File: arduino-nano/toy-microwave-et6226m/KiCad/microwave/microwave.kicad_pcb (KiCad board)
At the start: 4 copper layers, 76.2 x 165.1 mm, 60 parts, among them J1 Screw_Terminal_01x04, J2 Screw_Terminal_01x04, U1 AP63205WU, U2 CA56-12EWA

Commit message: fix(toy-microwave-et6226m): swap to a common-cathode display and drive the buzzer through a MOSFET
- What: U2 becomes CC56-12SURKWA, BZ1 moves low-side behind AO3400A Q2 with R9/R10 and SS14 flyback D18, D1-D16 are valued 1N4148W, U5 loads from the shared embedded library, and the BOM export is regenerated.
- Why: the ET6226M sources segments and sinks grids so a common-anode display never lights, and the 42 ohm coil drew about 119 mA from a pin rated 40 mA.
- How: pin-for-pin display swap on the same footprint, a gate-resistor and pull-down MOSFET stage clamped to +5V, and a project sym-lib-table pointing at kicad/embedded.kicad_sym.
- Benefit: the display lights, the buzzer no longer overloads D10, and ERC and DRC run clean.
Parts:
- added D18: SS14, Diode_SMD:D_SMA, B.Cu at (46.7, 29.2)
- added Q2: AO3400A, Package_TO_SOT_SMD:SOT-23, B.Cu at (41.7, 28.9)
- added R10: 4.7k, Resistor_SMD:R_0805_2012Metric_Pad1.20x1.40mm_HandSolder, B.Cu at (37.6, 30.3)
- added R9: 100, Resistor_SMD:R_0805_2012Metric_Pad1.20x1.40mm_HandSolder, B.Cu at (37.6, 27.9)
- D1, D10, D11, D12, D13, D14, D15, D16, D2, D3, D4, D5, D6, D7, D8, D9: value D_Small -> 1N4148W
- U2: value CA56-12EWA -> CC56-12SURKWA; footprint Display_7Segment:CA56-12EWA -> Display_7Segment:CA56-12SURKWA
- U5: value ~ -> ET6226M
- moved BZ1 7.33 mm to (59.7, 28.7), turned to 180 degrees
- moved U2 0.10 mm to (50.8, 55.6)
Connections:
- BZ1 pad 1: CTRL_BUZZER -> +5V
- BZ1 pad 2: GND -> Net-(BZ1--)
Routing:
- net +5V: track 137.0 -> 171.0 mm
- net CTRL_BUZZER: track 169.4 -> 153.6 mm, vias 0 -> 1
- net Net-(BZ1--): track 0.00 -> 12.0 mm
- net Net-(Q2-G): track 0.00 -> 4.51 mm

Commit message: refactor(toy-microwave-et6226m): resize the board to 3.0 x 6.5 in and place the display and keys to the enclosure template
- What: resizes the board outline to 3000 x 6500 mil and moves U2 (display) and MX1-MX16 (keys) to the positions in the imported enclosure DXF, with the schematic and project files resaved.
- Why: the enclosure template fixes where the display window and key cutouts sit, so the board has to match it.
- How: imported the template DXF as a reference and placed each part to its drawn position, keys on the 750 mil MX pitch.
- Benefit: display and key placement match the enclosure 1:1.
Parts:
- moved H1 13.0 mm to (98.1, 187.0)
- moved H2 9.84 mm to (98.1, 28.9)
- moved H4 9.84 mm to (28.9, 187.0)
- moved C5 8.98 mm to (89.7, 173.2)
- moved D15 8.98 mm to (76.2, 150.0)
- moved D13 8.98 mm to (38.1, 150.0)
- moved D14 8.98 mm to (57.1, 150.0)
- moved D16 8.98 mm to (95.2, 150.0)
- moved D3 8.98 mm to (76.2, 92.9)
- moved D7 8.98 mm to (76.2, 111.9)
- moved MX11 8.98 mm to (73.0, 130.2)
- moved MX12 8.98 mm to (92.1, 130.2)
- moved MX3 8.98 mm to (73.0, 92.1)
- moved MX4 8.98 mm to (92.1, 92.1)
- moved U1 8.98 mm to (86.9, 173.2)
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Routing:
- net SEG_DP: track 24.7 -> 30.2 mm
- net SEG_D/ROW3: track 192.2 -> 192.9 mm

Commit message: refactor(toy-microwave-et6226m): move the layout onto the mil standard
- What: sets every track to 10, 20, or 60 mil and every via to 24/12 mil, swaps H1-H4 to MountingHole_3.2mm_M3_ISO7380_Pad_TopBottom in the schematic and PCB, adds Default (10 mil) and Power (20 mil) net classes at 8 mil clearance, and adds 10/20/60 mil track and 24/12 mil via predefined sizes.
- Why: the board mixed 7.87, 9.84, 25, and 30 mil tracks with three via sizes, and the Pad_Via mounting holes sat 0.3 mm from the edge against a 0.5 mm rule.
- How: rescaled widths and vias in place, swapped each hole footprint at its existing position, and spread the 40 track pairs that sat at 0.2 mm to meet 8 mil clearance.
- Benefit: DRC reports 0 clearance, edge, and unconnected errors, and new tracks default to standard mil widths.
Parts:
- H1, H2, H3, H4: footprint MountingHole:MountingHole_3.2mm_M3_Pad_Via -> MountingHole:MountingHole_3.2mm_M3_ISO7380_Pad_TopBottom
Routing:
- net Net-(MX1-Pad1): track 114.6 -> 119.0 mm
- net DIG_CA2/COL1: track 50.3 -> 54.1 mm
- net DIG_CA3/COL2: track 56.7 -> 59.5 mm
- net Net-(MX12-Pad1): track 93.1 -> 95.3 mm
- net SEG_G: track 34.2 -> 35.8 mm
- net SEG_D/ROW3: track 192.9 -> 191.6 mm
- net SEG_C/ROW2: track 168.7 -> 167.4 mm
- net SEG_DP: track 30.2 -> 31.3 mm
- net DAT: track 155.2 -> 156.2 mm
- net SEG_B/ROW1: track 148.0 -> 147.1 mm
- net CLK: track 149.9 -> 150.7 mm
- net DIG_CA1/COL0: track 40.6 -> 41.3 mm

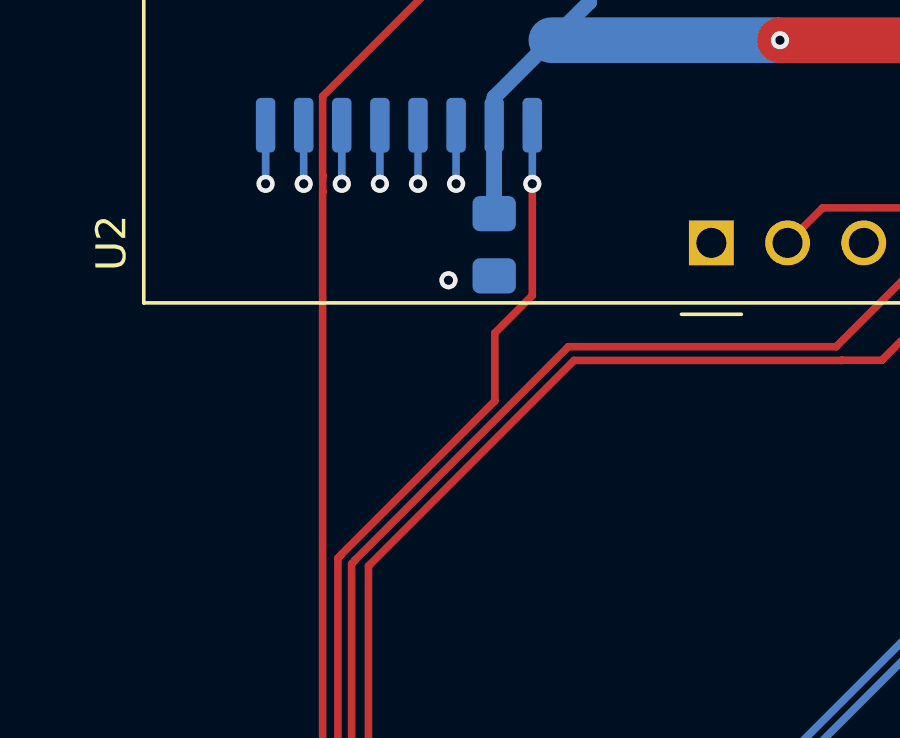
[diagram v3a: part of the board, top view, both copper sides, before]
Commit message: refactor(toy-microwave-et6226m): optimize segment connections in KiCad PCB layout
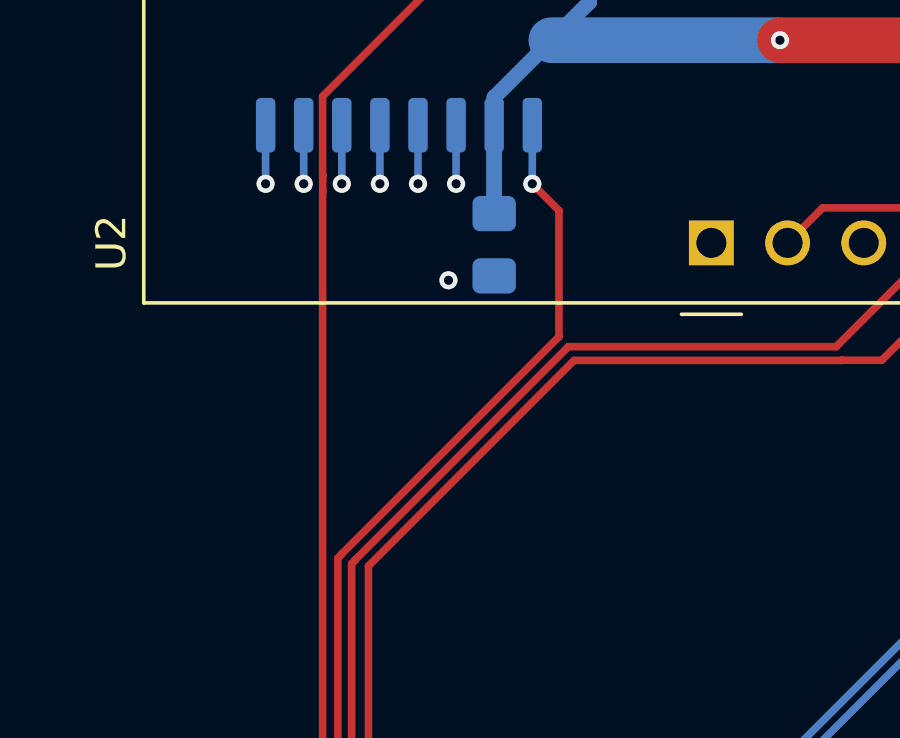
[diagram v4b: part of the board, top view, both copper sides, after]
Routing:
- net SEG_B/ROW1: track 147.1 -> 147.8 mm
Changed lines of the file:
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@@
 	)
 	(segment
-		(start 51.181 63.373)
-		(end 49.931199 64.622801)
+		(start 44.8056 72.022822)
+		(end 44.7008 72.127622)
 		(width 0.254)
 		(layer "F.Cu")
@@
 	)
 	(segment
-		(start 44.8056 72.022822)
-		(end 44.7008 72.127622)
+		(start 52.07 64.746843)
+		(end 44.8056 72.011243)
+		(width 0.254)
+		(layer "F.Cu")
+		(net "SEG_B{slash}ROW1")
+	)
+	(segment
+		(start 44.8056 72.011243)
+		(end 44.8056 72.022822)
 		(width 0.254)
 		(layer "F.Cu")
@@
 	)
 	(segment
+		(start 38.1 114.935)
+		(end 38.1 115.09375)
+		(width 0.254)
+		(layer "F.Cu")
+		(net "SEG_B{slash}ROW1")
+	)
+	(segment
 		(start 44.7008 108.3342)
 		(end 38.1 114.935)
@@
 	)
 	(segment
-		(start 49.931199 66.885645)
-		(end 44.8056 72.011243)
-		(width 0.254)
-		(layer "F.Cu")
-		(net "SEG_B{slash}ROW1")
-	)
-	(segment
-		(start 49.931199 64.622801)
-		(end 49.931199 66.885645)
-		(width 0.254)
-		(layer "F.Cu")
-		(net "SEG_B{slash}ROW1")
-	)
-	(segment
-		(start 44.8056 72.011243)
-		(end 44.8056 72.022822)
+		(start 52.07 60.5395)
+		(end 52.07 64.746843)
 		(width 0.254)
 		(layer "F.Cu")
@@
 	(segment
 		(start 51.181 59.6505)
-		(end 51.181 63.373)
+		(end 52.07 60.5395)
 		(width 0.254)
 		(layer "F.Cu")
-		(net "SEG_B{slash}ROW1")
-	)
-	(segment
-		(start 38.1 114.935)
-		(end 38.1 115.09375)
-		(width 0.254)
-		(layer "F.Cu")

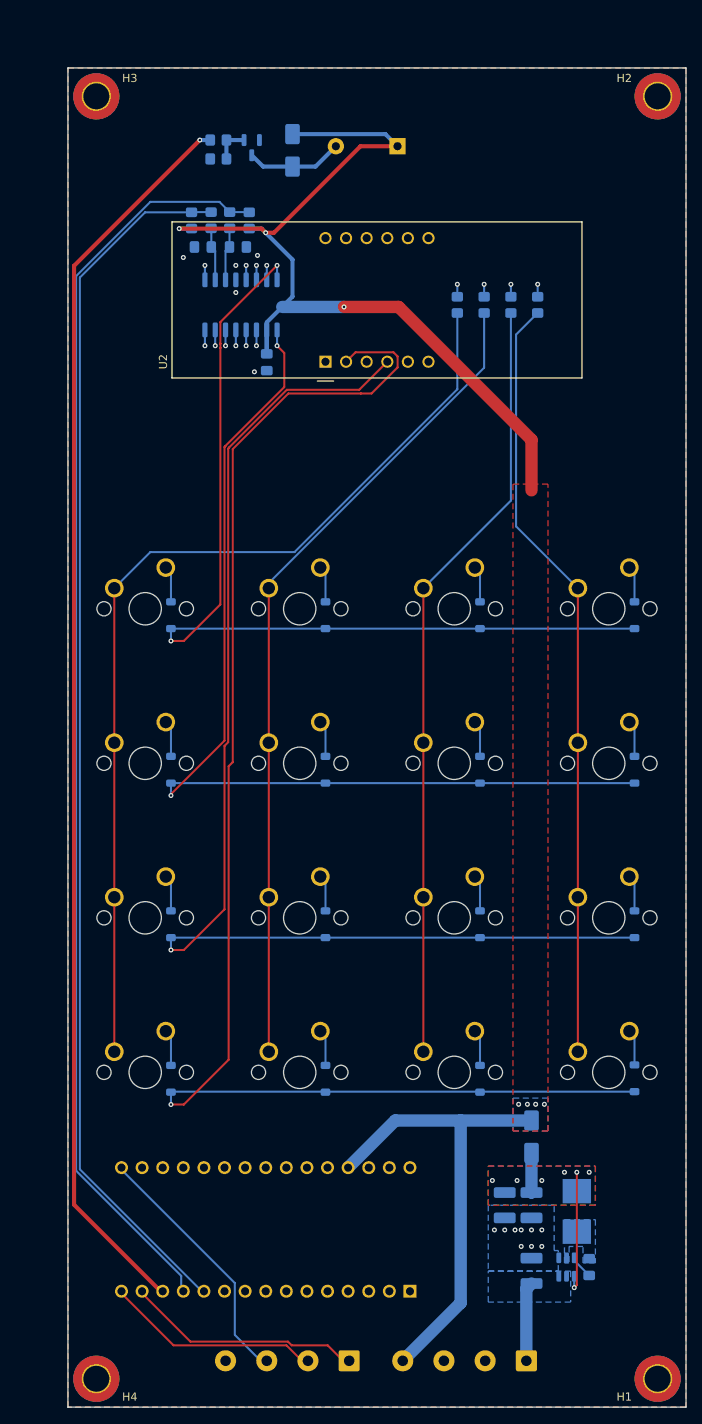
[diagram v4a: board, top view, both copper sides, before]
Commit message: refactor(toy-microwave-et6226m): reroute the board on 2 layers
- What: drops the stackup from 4 to 2 copper layers, moves U5 between the display pin rows with C3 and the CLK/DAT parts at its ends, reroutes the display, matrix, and +5V nets on F.Cu and B.Cu, and replaces the +5V strip pour with a 20 mil trunk from D17.
- Why: the inner layers carried 13 signal nets rather than planes, and U5 sat left of the display pins so every segment and digit net crossed the others.
- How: kept every pin assignment so firmware is unchanged, used the display's through-hole pins as layer changes, routed CLK and DAT under U5, ran DAT high so the GND pocket under U5 joins the main pour, and stitched the buck GND pour to the main plane.
- Benefit: DRC reports 0 unconnected pads, 0 clearance errors, and 43 vias all at 24/12 mil, with the display cluster using 11 signal vias instead of 20.
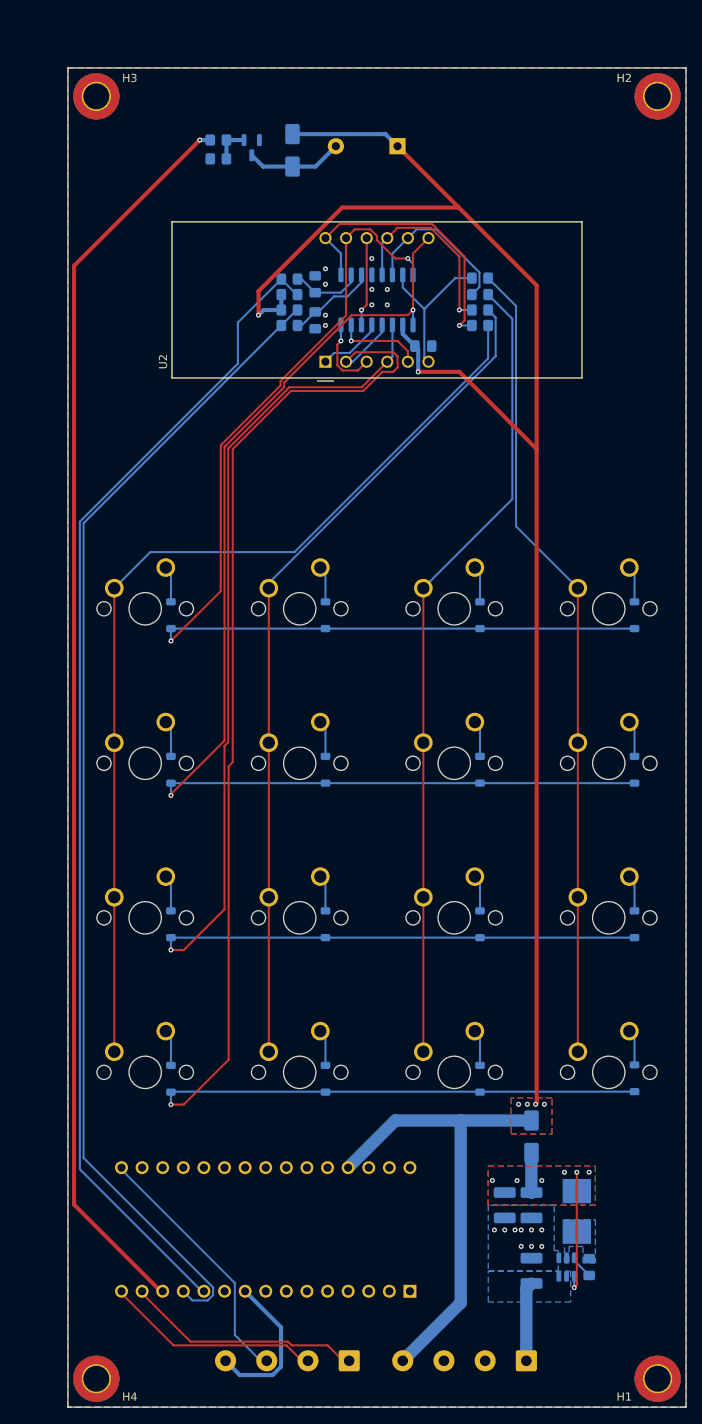
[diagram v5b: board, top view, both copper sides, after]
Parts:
- moved C3 19.4 mm to (69.2, 59.7), turned to 0 degrees
- moved U5 16.8 mm to (63.5, 54.0)
- moved R8 15.1 mm to (52.7, 53.3), turned to 0 degrees
- moved R5 14.9 mm to (52.7, 57.1), turned to 0 degrees
- moved C2 14.6 mm to (55.9, 52.1), turned to 90 degrees
- moved C1 13.1 mm to (55.9, 56.5), turned to -90 degrees
- moved R7 12.1 mm to (52.7, 55.2), turned to 0 degrees
- moved R6 12.1 mm to (52.7, 51.4), turned to 0 degrees
- moved R4 7.84 mm to (76.2, 51.3), turned to 0 degrees
- moved R3 4.02 mm to (76.2, 53.3), turned to 0 degrees
- moved R1 3.78 mm to (76.2, 57.1), turned to 0 degrees
- moved R2 0.81 mm to (76.2, 55.2), turned to 0 degrees
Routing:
- net +5V: track 170.8 -> 258.4 mm, vias 7 -> 6
- net DIG_CA3/COL2: track 59.5 -> 19.9 mm, vias 2 -> 0
- net DIG_CA2/COL1: track 54.1 -> 23.8 mm, vias 2 -> 1
- net DIG_CA4/COL3: track 47.4 -> 19.5 mm, vias 2 -> 0
- net SEG_G: track 35.8 -> 11.1 mm
- net SEG_DP: track 31.3 -> 9.49 mm
- net SEG_C/ROW2: track 167.4 -> 153.2 mm, vias 2 -> 1
- net SEG_F: track 24.9 -> 11.0 mm
- net DAT: track 156.2 -> 143.4 mm
- net CTRL_MISC: track 9.57 -> 19.1 mm
- net SEG_D/ROW3: track 191.6 -> 183.3 mm, vias 2 -> 1
- net CLK: track 150.7 -> 144.1 mm
- net SEG_A/ROW0: track 123.1 -> 129.4 mm
- net DIG_CA1/COL0: track 41.3 -> 35.1 mm, vias 2 -> 1
- net SEG_E: track 13.8 -> 8.02 mm, vias 1 -> 0
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- removed copper zone on In1.Cu, net GND
- removed copper zone on In2.Cu, net GND
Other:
- copper layers 4 -> 2
